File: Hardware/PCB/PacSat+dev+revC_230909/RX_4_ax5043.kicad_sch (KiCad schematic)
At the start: 20 parts, among them U151 RFShield_OnePiece, U505 AX5043

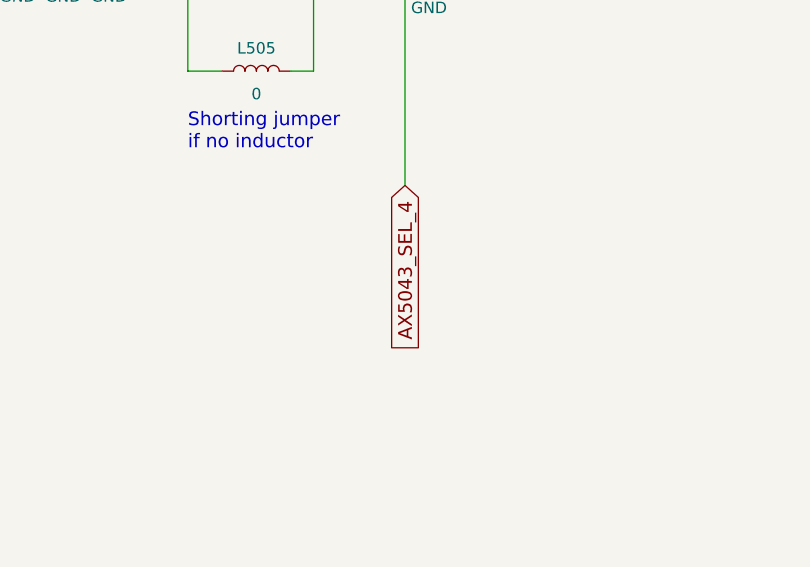
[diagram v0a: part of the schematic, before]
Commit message: Changed schematic to add Select lines for each AX5043 on the CPU.
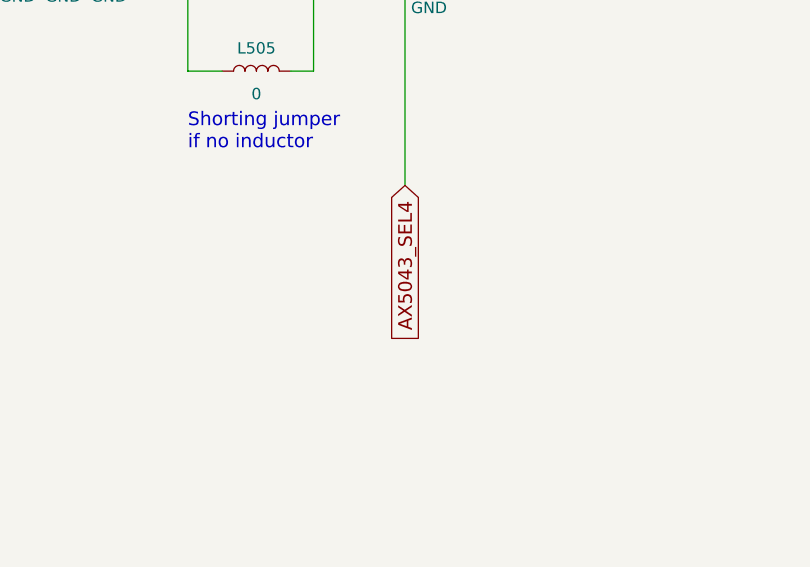
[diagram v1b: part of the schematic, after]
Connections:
- net AX5043_SEL_4 renamed AX5043_SEL4
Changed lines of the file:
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@@
     )
   )
-  (global_label "AX5043_SEL_4" (shape input) (at 224.79 184.15 270) (fields_autoplaced)
+  (global_label "AX5043_SEL4" (shape input) (at 224.79 184.15 270) (fields_autoplaced)
     (effects (font (size 1.524 1.524)) (justify right))
-    (property "Intersheetrefs" "${INTERSHEET_REFS}" (at 224.79 203.2523 90)
+    (property "Intersheetrefs" "${INTERSHEET_REFS}" (at 224.79 202.1866 90)
       (effects (font (size 1.524 1.524)) (justify right) hide)
     )
@@
     (pin "1")
     (instances
-      (project "pACsAT_dEV_rEVc_230907"
+      (project "PacSat+dev+revC_230909"
         (path "/cc9f42d2-6985-41ac-acab-5ab7b01c5b38/f99c6a69-4136-42a1-b9ff-80c66d5e136e"
           (reference "#PWR0503") (unit 1)
@@
     (pin "2")
     (instances
-      (project "pACsAT_dEV_rEVc_230907"
+      (project "PacSat+dev+revC_230909"
         (path "/cc9f42d2-6985-41ac-acab-5ab7b01c5b38/f99c6a69-4136-42a1-b9ff-80c66d5e136e"
           (reference "C501") (unit 1)
@@
     (pin "2")
     (instances
-      (project "pACsAT_dEV_rEVc_230907"
+      (project "PacSat+dev+revC_230909"
         (path "/cc9f42d2-6985-41ac-acab-5ab7b01c5b38/00000000-0000-0000-0000-00005a014be3"
           (reference "L152") (unit 1)
@@
     (pin "1")
     (instances
-      (project "pACsAT_dEV_rEVc_230907"
+      (project "PacSat+dev+revC_230909"
         (path "/cc9f42d2-6985-41ac-acab-5ab7b01c5b38/f99c6a69-4136-42a1-b9ff-80c66d5e136e"
           (reference "#PWR0512") (unit 1)
@@
     (pin "2")
     (instances
-      (project "pACsAT_dEV_rEVc_230907"
+      (project "PacSat+dev+revC_230909"
         (path "/cc9f42d2-6985-41ac-acab-5ab7b01c5b38/07d62cf1-e888-4b13-86c4-67d770627579"
           (reference "R88") (unit 1)
@@
     (pin "2")
     (instances
-      (project "pACsAT_dEV_rEVc_230907"
+      (project "PacSat+dev+revC_230909"
         (path "/cc9f42d2-6985-41ac-acab-5ab7b01c5b38/f99c6a69-4136-42a1-b9ff-80c66d5e136e"
           (reference "L505") (unit 1)
@@
     (pin "2")
     (instances
-      (project "pACsAT_dEV_rEVc_230907"
+      (project "PacSat+dev+revC_230909"
         (path "/cc9f42d2-6985-41ac-acab-5ab7b01c5b38/00000000-0000-0000-0000-00005a014be3"
           (reference "C711") (unit 1)
@@
     (pin "2")
     (instances
-      (project "pACsAT_dEV_rEVc_230907"
+      (project "PacSat+dev+revC_230909"
         (path "/cc9f42d2-6985-41ac-acab-5ab7b01c5b38/00000000-0000-0000-0000-00005a014be3"
           (reference "C712") (unit 1)
@@
     (pin "2")
     (instances
-      (project "pACsAT_dEV_rEVc_230907"
+      (project "PacSat+dev+revC_230909"
         (path "/cc9f42d2-6985-41ac-acab-5ab7b01c5b38/f99c6a69-4136-42a1-b9ff-80c66d5e136e"
           (reference "C502") (unit 1)
@@
     (pin "1")
     (instances
-      (project "pACsAT_dEV_rEVc_230907"
+      (project "PacSat+dev+revC_230909"
         (path "/cc9f42d2-6985-41ac-acab-5ab7b01c5b38/00000000-0000-0000-0000-00005a014be3"
           (reference "#PWR0161") (unit 1)
@@
     (pin "1")
     (instances
-      (project "pACsAT_dEV_rEVc_230907"
+      (project "PacSat+dev+revC_230909"
         (path "/cc9f42d2-6985-41ac-acab-5ab7b01c5b38/9af0eacb-5211-4e23-85d7-9c1805bbe6a4"
           (reference "#PWR0614") (unit 1)
@@
     (pin "1")
     (instances
-      (project "pACsAT_dEV_rEVc_230907"
+      (project "PacSat+dev+revC_230909"
         (path "/cc9f42d2-6985-41ac-acab-5ab7b01c5b38/f99c6a69-4136-42a1-b9ff-80c66d5e136e"
           (reference "#PWR0504") (unit 1)
@@
     (pin "2")
     (instances
-      (project "pACsAT_dEV_rEVc_230907"
+      (project "PacSat+dev+revC_230909"
         (path "/cc9f42d2-6985-41ac-acab-5ab7b01c5b38/00000000-0000-0000-0000-00005a014be3"
           (reference "L152") (unit 1)
@@
     (pin "1")
     (instances
-      (project "pACsAT_dEV_rEVc_230907"
+      (project "PacSat+dev+revC_230909"
         (path "/cc9f42d2-6985-41ac-acab-5ab7b01c5b38/f99c6a69-4136-42a1-b9ff-80c66d5e136e"
           (reference "#PWR0507") (unit 1)
@@
     (pin "1")
     (instances
-      (project "pACsAT_dEV_rEVc_230907"
+      (project "PacSat+dev+revC_230909"
         (path "/cc9f42d2-6985-41ac-acab-5ab7b01c5b38/07d62cf1-e888-4b13-86c4-67d770627579"
           (reference "#PWR0191") (unit 1)
@@
     (pin "2")
     (instances
-      (project "pACsAT_dEV_rEVc_230907"
+      (project "PacSat+dev+revC_230909"
         (path "/cc9f42d2-6985-41ac-acab-5ab7b01c5b38/00000000-0000-0000-0000-00005a014be3"
           (reference "L152") (unit 1)
@@
     (pin "1")
     (instances
-      (project "pACsAT_dEV_rEVc_230907"
+      (project "PacSat+dev+revC_230909"
         (path "/cc9f42d2-6985-41ac-acab-5ab7b01c5b38/00000000-0000-0000-0000-00005a014be3"
           (reference "#PWR0735") (unit 1)
@@
     (pin "1")
     (instances
-      (project "pACsAT_dEV_rEVc_230907"
+      (project "PacSat+dev+revC_230909"
         (path "/cc9f42d2-6985-41ac-acab-5ab7b01c5b38/f99c6a69-4136-42a1-b9ff-80c66d5e136e"
           (reference "#PWR0511") (unit 1)
@@
     (pin "3")
     (instances
-      (project "pACsAT_dEV_rEVc_230907"
+      (project "PacSat+dev+revC_230909"
         (path "/cc9f42d2-6985-41ac-acab-5ab7b01c5b38/9af0eacb-5211-4e23-85d7-9c1805bbe6a4"
           (reference "U605") (unit 1)
@@
     (pin "2")
     (instances
-      (project "pACsAT_dEV_rEVc_230907"
+      (project "PacSat+dev+revC_230909"
         (path "/cc9f42d2-6985-41ac-acab-5ab7b01c5b38/f99c6a69-4136-42a1-b9ff-80c66d5e136e"
           (reference "C503") (unit 1)
@@
     (pin "1")
     (instances
-      (project "pACsAT_dEV_rEVc_230907"
+      (project "PacSat+dev+revC_230909"
         (path "/cc9f42d2-6985-41ac-acab-5ab7b01c5b38/f99c6a69-4136-42a1-b9ff-80c66d5e136e"
           (reference "#PWR0506") (unit 1)
@@
     (pin "1")
     (instances
-      (project "pACsAT_dEV_rEVc_230907"
+      (project "PacSat+dev+revC_230909"
         (path "/cc9f42d2-6985-41ac-acab-5ab7b01c5b38/00000000-0000-0000-0000-00005a014be3"
           (reference "#PWR0161") (unit 1)
@@
     (pin "1")
     (instances
-      (project "pACsAT_dEV_rEVc_230907"
+      (project "PacSat+dev+revC_230909"
         (path "/cc9f42d2-6985-41ac-acab-5ab7b01c5b38/00000000-0000-0000-0000-00005a014be3"
           (reference "#PWR0161") (unit 1)
@@
     (pin "2")
     (instances
-      (project "pACsAT_dEV_rEVc_230907"
+      (project "PacSat+dev+revC_230909"
         (path "/cc9f42d2-6985-41ac-acab-5ab7b01c5b38/f99c6a69-4136-42a1-b9ff-80c66d5e136e"
           (reference "C504") (unit 1)
@@
     (pin "5")
     (instances
-      (project "pACsAT_dEV_rEVc_230907"
+      (project "PacSat+dev+revC_230909"
         (path "/cc9f42d2-6985-41ac-acab-5ab7b01c5b38/00000000-0000-0000-0000-00005a014be3"
           (reference "U151") (unit 1)
@@
     (pin "3")
     (instances
-      (project "pACsAT_dEV_rEVc_230907"
+      (project "PacSat+dev+revC_230909"
         (path "/cc9f42d2-6985-41ac-acab-5ab7b01c5b38/9af0eacb-5211-4e23-85d7-9c1805bbe6a4"
           (reference "U607") (unit 1)
@@
     (pin "1")
     (instances
-      (project "pACsAT_dEV_rEVc_230907"
+      (project "PacSat+dev+revC_230909"
         (path "/cc9f42d2-6985-41ac-acab-5ab7b01c5b38/00000000-0000-0000-0000-00005a014be3"
           (reference "#PWR0161") (unit 1)
@@
     (pin "1")
     (instances
-      (project "pACsAT_dEV_rEVc_230907"
+      (project "PacSat+dev+revC_230909"
         (path "/cc9f42d2-6985-41ac-acab-5ab7b01c5b38/f99c6a69-4136-42a1-b9ff-80c66d5e136e"
           (reference "#PWR0514") (unit 1)
@@
     (pin "2")
     (instances
-      (project "pACsAT_dEV_rEVc_230907"
+      (project "PacSat+dev+revC_230909"
         (path "/cc9f42d2-6985-41ac-acab-5ab7b01c5b38/f99c6a69-4136-42a1-b9ff-80c66d5e136e"
           (reference "R503") (unit 1)
@@
     (pin "1")
     (instances
-      (project "pACsAT_dEV_rEVc_230907"
+      (project "PacSat+dev+revC_230909"
         (path "/cc9f42d2-6985-41ac-acab-5ab7b01c5b38/f99c6a69-4136-42a1-b9ff-80c66d5e136e"
           (reference "#PWR0513") (unit 1)
@@
     (pin "2")
     (instances
-      (project "pACsAT_dEV_rEVc_230907"
+      (project "PacSat+dev+revC_230909"
         (path "/cc9f42d2-6985-41ac-acab-5ab7b01c5b38/00000000-0000-0000-0000-00005a014be3"
           (reference "L152") (unit 1)
@@
     (pin "1")
     (instances
-      (project "pACsAT_dEV_rEVc_230907"
+      (project "PacSat+dev+revC_230909"
         (path "/cc9f42d2-6985-41ac-acab-5ab7b01c5b38/f99c6a69-4136-42a1-b9ff-80c66d5e136e"
           (reference "#PWR0508") (unit 1)
@@
     (pin "9")
     (instances
-      (project "pACsAT_dEV_rEVc_230907"
+      (project "PacSat+dev+revC_230909"
         (path "/cc9f42d2-6985-41ac-acab-5ab7b01c5b38/f99c6a69-4136-42a1-b9ff-80c66d5e136e"
           (reference "U505") (unit 1)
@@
     (pin "1")
     (instances
-      (project "pACsAT_dEV_rEVc_230907"
+      (project "PacSat+dev+revC_230909"
         (path "/cc9f42d2-6985-41ac-acab-5ab7b01c5b38/f99c6a69-4136-42a1-b9ff-80c66d5e136e"
           (reference "#PWR0510") (unit 1)
@@
     (pin "2")
     (instances
-      (project "pACsAT_dEV_rEVc_230907"
+      (project "PacSat+dev+revC_230909"
         (path "/cc9f42d2-6985-41ac-acab-5ab7b01c5b38/f99c6a69-4136-42a1-b9ff-80c66d5e136e"
           (reference "C508") (unit 1)
@@
     (pin "1")
     (instances
-      (project "pACsAT_dEV_rEVc_230907"
+      (project "PacSat+dev+revC_230909"
         (path "/cc9f42d2-6985-41ac-acab-5ab7b01c5b38/00000000-0000-0000-0000-00005a014be3"
           (reference "#PWR0161") (unit 1)
@@
     (pin "2")
     (instances
-      (project "pACsAT_dEV_rEVc_230907"
+      (project "PacSat+dev+revC_230909"
         (path "/cc9f42d2-6985-41ac-acab-5ab7b01c5b38/f99c6a69-4136-42a1-b9ff-80c66d5e136e"
           (reference "R502") (unit 1)
@@
     (pin "2")
     (instances
-      (project "pACsAT_dEV_rEVc_230907"
+      (project "PacSat+dev+revC_230909"
         (path "/cc9f42d2-6985-41ac-acab-5ab7b01c5b38/f99c6a69-4136-42a1-b9ff-80c66d5e136e"
           (reference "C505") (unit 1)
